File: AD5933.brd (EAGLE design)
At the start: 101.6 x 53.4 mm, 80 parts, among them U1 ADG1604BRUZ, U10 ADP3303ARZ-3.3, U11 AD5242BRZ1M, U12 AD5245BRJZ100-R2, U2 AD5933YRSZ, U3 AD5242BRZ1M, U4 AD8606ARZ, U5 ADG1604BRUZ, U7 AD8606ARZ, U8 LTC6904MPMS8TRPBF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

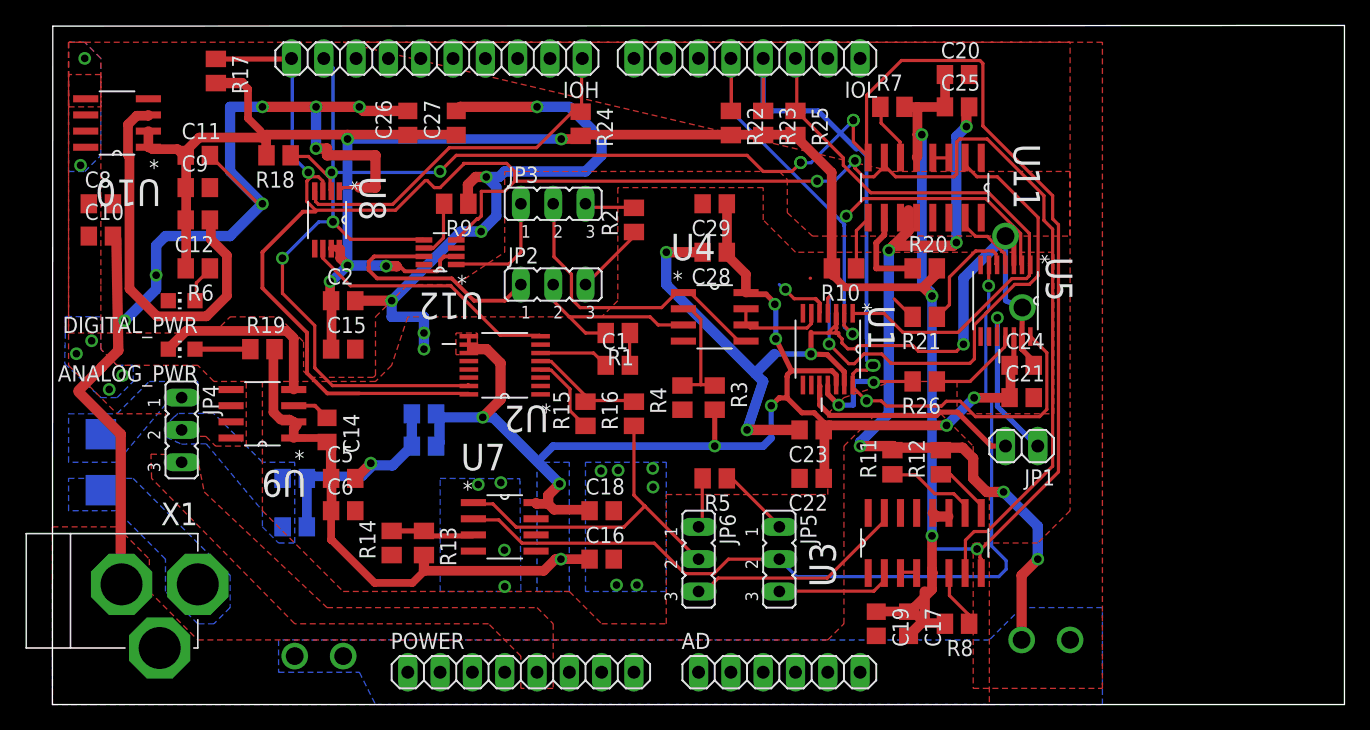
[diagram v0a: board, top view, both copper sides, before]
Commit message: complete DRC in layout
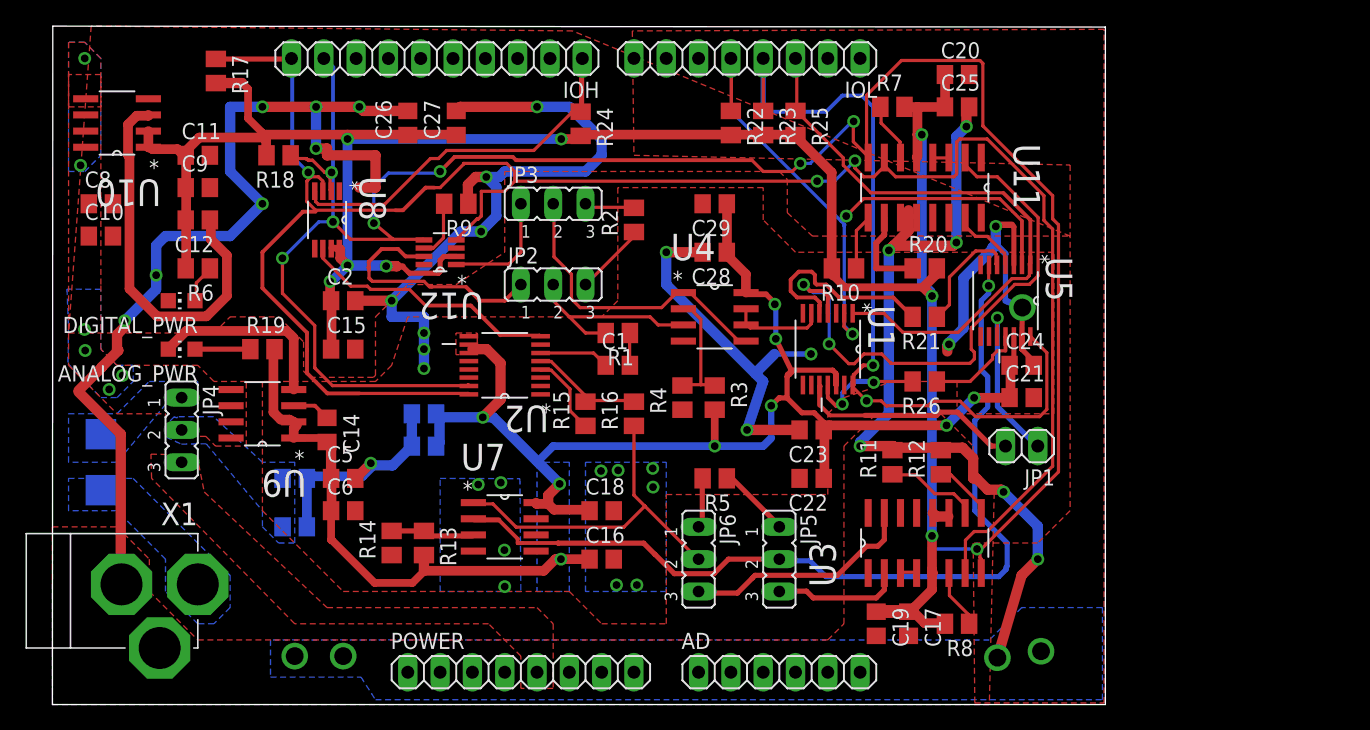
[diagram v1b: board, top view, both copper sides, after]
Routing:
- net AGND: track 109.8 -> 92.4 mm, vias 18 -> 19
- net GND: track 210.2 -> 195.6 mm
- net U1_S2: track 7.18 -> 16.1 mm, vias 1 -> 0
- net U1_S1: track 39.9 -> 46.5 mm, vias 1 -> 2
- net A11: track 60.7 -> 64.3 mm, vias 3 -> 2
- net EN1: track 50.4 -> 52.9 mm
- net SDA: track 165.5 -> 167.4 mm, vias 7 -> 8
- net U3_W2: track 17.5 -> 19.0 mm
- net U7_INA-: track 69.7 -> 71.1 mm
- net U3_A1: track 9.21 -> 10.1 mm
- net U12_B: track 18.7 -> 19.6 mm
- net A01: track 46.7 -> 47.4 mm
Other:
- board size 101.6 x 53.4 mm -> 82.8 x 53.3 mm
